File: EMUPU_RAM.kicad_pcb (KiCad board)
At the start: 2 copper layers, 99.1 x 82.5 mm, 30 parts, among them J1 Conn_01x20_Socket, J2 Conn_01x20_Socket, J3 Barrel_Jack_Switch, J4 Conn_01x06_Pin, J5 Conn_01x08_Pin, J6 Conn_01x06_Pin, J7 Conn_01x02_Pin, SW1 SW_SPDT, SW2 SW_SPST, U2 HM678127_SOJ32_Arranged, U3 PIC18F57Q43-IPT

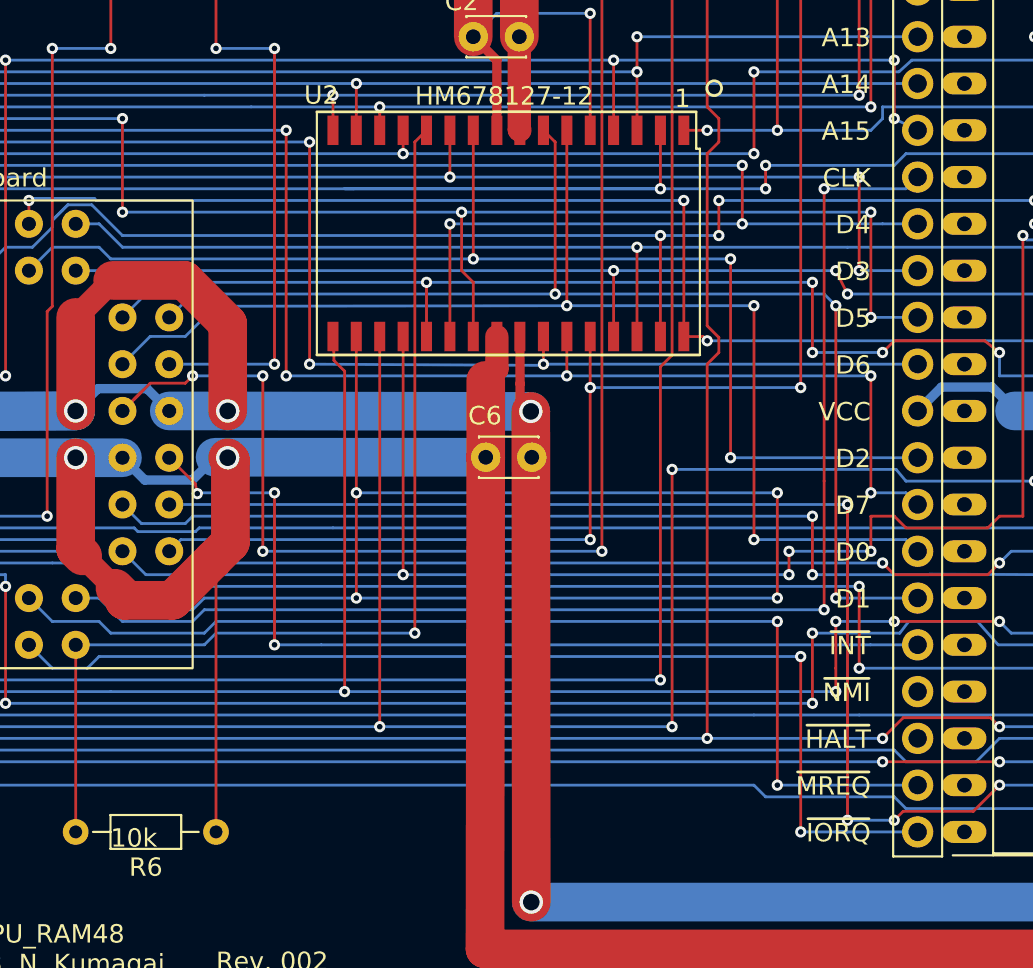
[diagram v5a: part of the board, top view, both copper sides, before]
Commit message: RAM48 pcb slightly revised
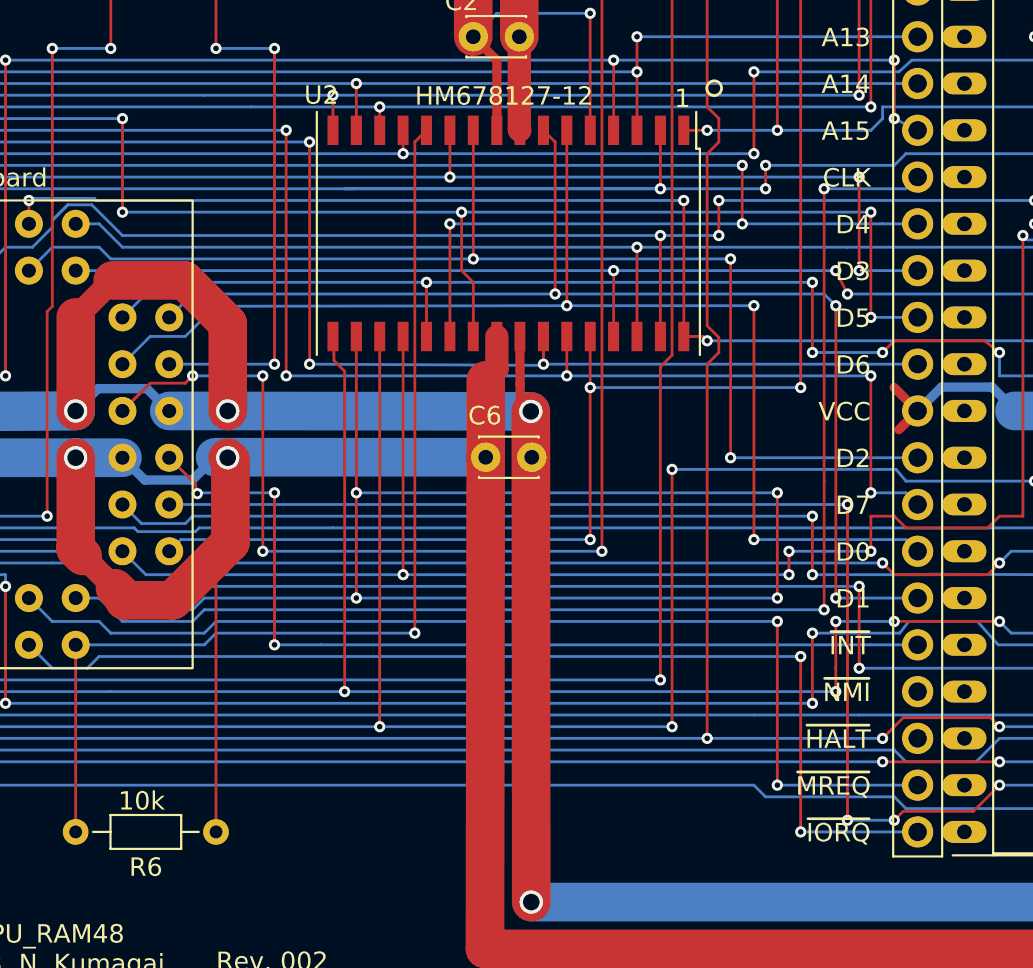
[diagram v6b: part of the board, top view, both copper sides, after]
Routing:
- net VCC: track 353.6 -> 358.6 mm
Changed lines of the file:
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@@
     )
   )
-  (gr_line (start 117.235 92.98) (end 137.835 92.98)
-    (stroke (width 0.15) (type default)) (layer "F.SilkS"))
   (gr_poly
     (pts
@@
   (gr_circle (center 138.811 91.694) (end 138.938 92.075)
     (stroke (width 0.15) (type default)) (fill none) (layer "F.SilkS"))
-  (gr_line (start 117.235 106.18) (end 138.035 106.18)
-    (stroke (width 0.15) (type default)) (layer "F.SilkS"))
   (gr_line (start 182.88 58.42) (end 182.88 140.97)
     (stroke (width 0.1) (type solid)) (layer "Edge.Cuts"))
@@
     (effects (font (size 1 1) (thickness 0.15)) (justify right bottom))
   )
-  (gr_text "10k" (at 106.03 133) (layer "F.SilkS")
+  (gr_text "10k" (at 106.4514 130.9878) (layer "F.SilkS")
     (effects (font (size 1 1) (thickness 0.15)) (justify left bottom))
   )
@@
   (segment (start 111.76 132.08) (end 111.76 117.475) (width 0.1524) (layer "F.Cu") (net 1))
   (segment (start 158.75 138.43) (end 126.365 138.43) (width 2.1) (layer "F.Cu") (net 1))
+  (segment (start 149.86 109.22) (end 148.59 107.95) (width 0.508) (layer "F.Cu") (net 1))
   (segment (start 119.38 67.31) (end 109.22 67.31) (width 2.1) (layer "F.Cu") (net 1))
   (segment (start 125.729806 71.199806) (end 125.729806 67.31) (width 2.1) (layer "F.Cu") (net 1))
@@
   (segment (start 111.76 117.475) (end 111.591663 117.306663) (width 0.1524) (layer "F.Cu") (net 1))
   (segment (start 158.75 72.77) (end 160.02 71.5) (width 2.1) (layer "F.Cu") (net 1))
+  (segment (start 148.844 110.236) (end 148.59 110.236) (width 0.1524) (layer "F.Cu") (net 1))
+  (segment (start 149.86 109.22) (end 148.844 108.204) (width 0.1524) (layer "F.Cu") (net 1))
   (segment (start 158.7246 109.22) (end 158.75 109.2454) (width 2.1) (layer "F.Cu") (net 1))
+  (segment (start 148.844 110.236) (end 149.86 109.22) (width 0.508) (layer "F.Cu") (net 1))
   (segment (start 160.02 71.5) (end 160.02 69.85) (width 2.1) (layer "F.Cu") (net 1))
   (segment (start 128.23 88.9) (end 128.23 91.821) (width 1.27) (layer "F.Cu") (net 1))
@@
     (connect_pads (clearance 0.35))
     (min_thickness 0.254) (filled_areas_thickness no)
-    (fill (thermal_gap 0.5) (thermal_bridge_width 0.508))
+    (fill yes (thermal_gap 0.5) (thermal_bridge_width 0.508))
     (polygon
       (pts
@@
     (connect_pads (clearance 0.35))
     (min_thickness 0.25) (filled_areas_thickness no)
-    (fill (thermal_gap 0.5) (thermal_bridge_width 0.5))
+    (fill yes (thermal_gap 0.5) (thermal_bridge_width 0.5))
     (polygon
       (pts
